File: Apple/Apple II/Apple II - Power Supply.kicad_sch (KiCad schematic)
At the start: 0 parts

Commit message: Working on Apple II - Sheet 23
My eyes said I need a break :smile:
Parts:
- added C1, C2: C_Polarized_Small, symbol Device:C_Polarized_Small
- added C23, C3, C4, C5: C_Small, symbol Device:C_Small
- added CR1: CR1_BRIDGE_RECTIFIER, symbol Apple II:CR1_BRIDGE_RECTIFIER
- added CR2, CR3: D_Filled, symbol Device:D_Filled
- added FU1: Fuse, symbol Device:Fuse
- added LF?: LINE_FILTER, symbol Apple II:LINE_FILTER
- added Q3: 2N2219, Package_TO_SOT_THT:TO-39-3, symbol Transistor_BJT:2N2219
- added R1, R2, R23, R3, R4: R_US, symbol Device:R_US
- added TR?: TR0001_TRANSFORMER, symbol Apple II:TR0001_TRANSFORMER
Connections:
- new net: C1.2, C2.2, C3.2, CR1., CR2.1 (K)
- new net: CR2.2 (A), R2.2, R3.1
- new net: C23.1, R23.1
- new net: R23.2, TR?.
- new net: Q3.1 (E), R3.2
- new net: C4.2, Q3.3 (C), TR?.
- new net: C3.1, CR3.1 (K), FU1.2, R4.2, TR?.
- new net: C23.2, CR3.2 (A), TR?.
- new net: C4.1, R4.1
- new net: C1.1, C2.1, CR1., FU1.1
- new net: C5.1, CR1., LF?.
- new net: C5.2, R2.1
- new net: LF?., R1.1
- new net: CR1., R1.2
- new net AC: LF?.
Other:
- title: (none) -> Apple II - Power Supply

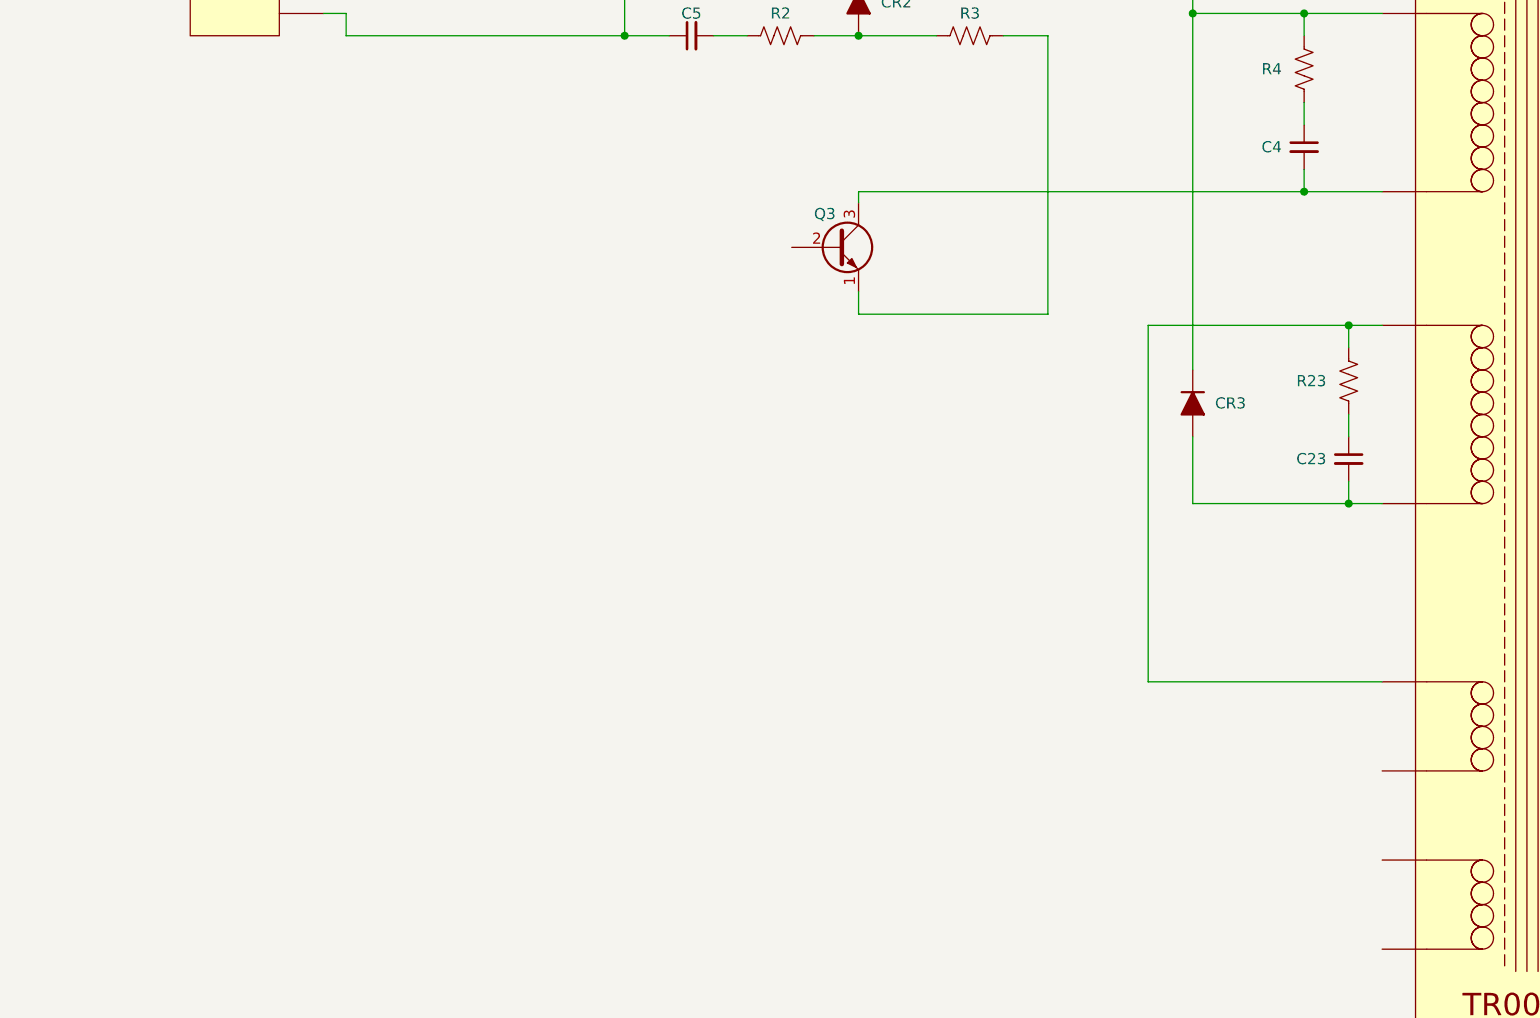
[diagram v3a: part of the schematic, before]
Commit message: Working on the Apple II Sheet 23
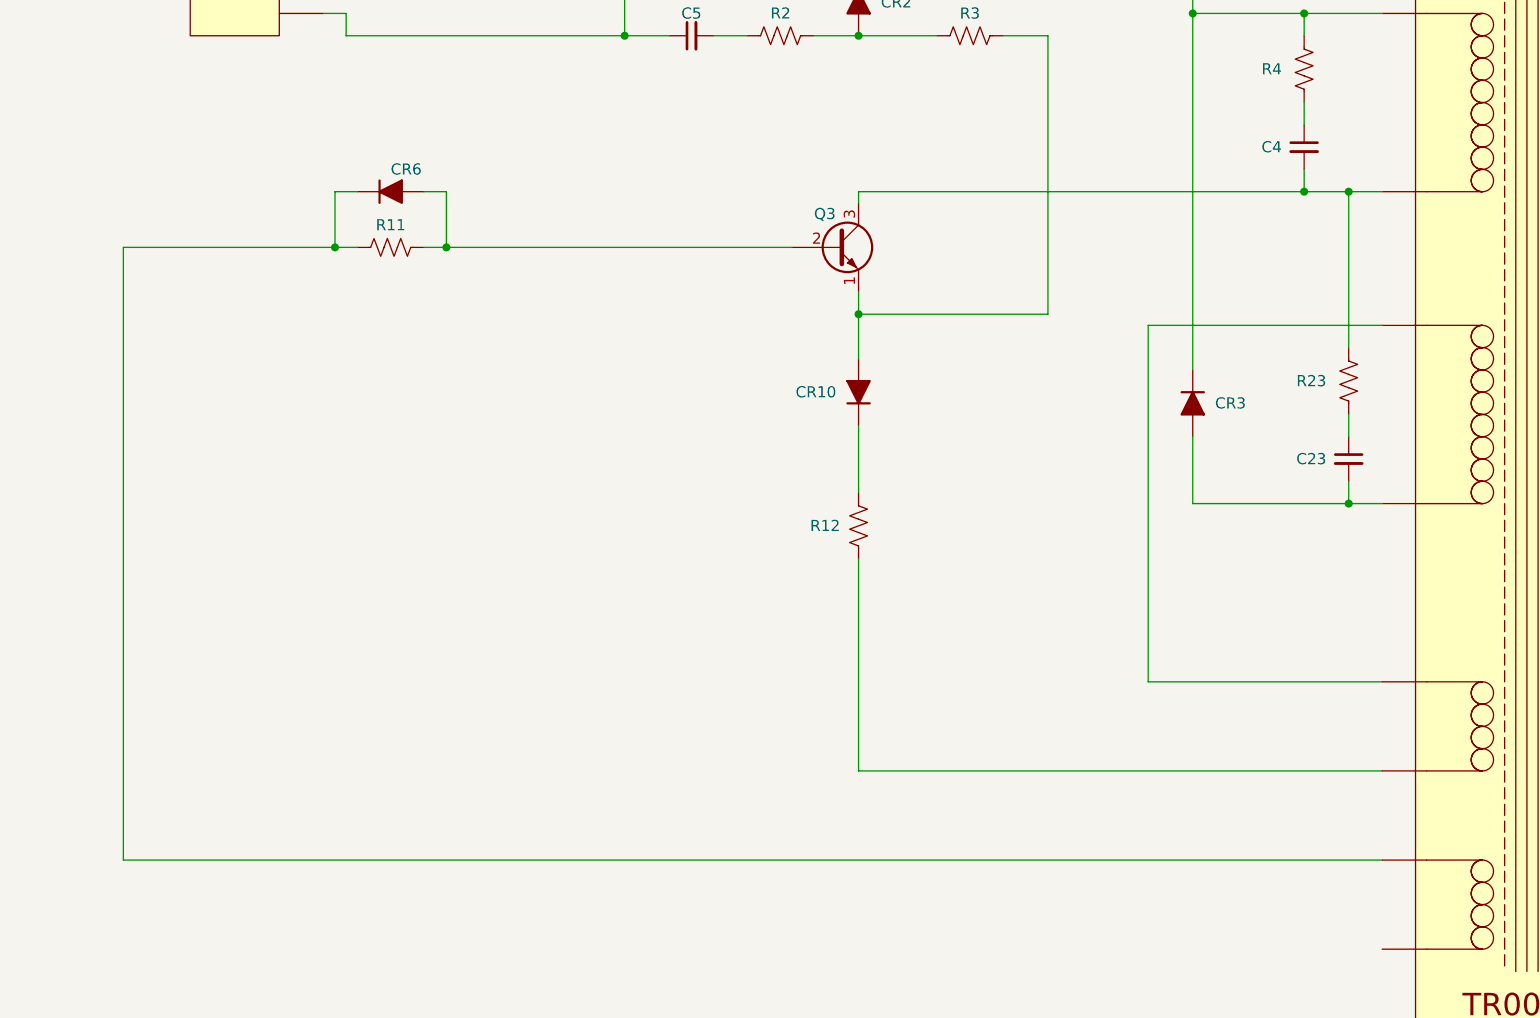
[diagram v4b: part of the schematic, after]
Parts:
- added CR10, CR6: D_Filled, symbol Device:D_Filled
- added R11, R12: R_US, symbol Device:R_US
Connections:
- net at R23.2, TR?.: now also C4.2, Q3.3 (C)
- net at Q3.1 (E), R3.2: now also CR10.2 (A)
- net at Q3.2 (B): now also CR6.2 (A), R11.2
- net at TR?.: now also CR6.1 (K), R11.1
- new net: R12.1, TR?.
- new net: CR10.1 (K), R12.2
- new net: C5.1, CR1., LF?.
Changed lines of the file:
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@@
   (junction (at 109.22 81.28) (diameter 0) (color 0 0 0 0)
   )
+  (junction (at 62.23 115.57) (diameter 0) (color 0 0 0 0)
+  )
   (junction (at 165.1 144.78) (diameter 0) (color 0 0 0 0)
   )
   (junction (at 114.3 66.04) (diameter 0) (color 0 0 0 0)
   )
+  (junction (at 109.22 123.19) (diameter 0) (color 0 0 0 0)
+  )
+  (junction (at 165.1 109.22) (diameter 0) (color 0 0 0 0)
+  )
   (junction (at 82.55 91.44) (diameter 0) (color 0 0 0 0)
   )
@@
   (junction (at 114.3 81.28) (diameter 0) (color 0 0 0 0)
   )
-  (junction (at 165.1 124.46) (diameter 0) (color 0 0 0 0)
+  (junction (at 49.53 115.57) (diameter 0) (color 0 0 0 0)
   )
   (wire (pts (xy 50.8 66.04) (xy 53.34 66.04))
@@
     (stroke (width 0) (type default) (color 0 0 0 0))
   )
+  (wire (pts (xy 52.07 115.57) (xy 49.53 115.57))
+    (stroke (width 0) (type default) (color 0 0 0 0))
+  )
   (wire (pts (xy 147.32 76.2) (xy 147.32 66.04))
     (stroke (width 0) (type default) (color 0 0 0 0))
   )
+  (wire (pts (xy 109.22 175.26) (xy 109.22 151.13))
+    (stroke (width 0) (type default) (color 0 0 0 0))
+  )
   (wire (pts (xy 50.8 68.58) (xy 48.26 68.58))
     (stroke (width 0) (type default) (color 0 0 0 0))
@@
     (stroke (width 0) (type default) (color 0 0 0 0))
   )
+  (wire (pts (xy 62.23 115.57) (xy 59.69 115.57))
+    (stroke (width 0) (type default) (color 0 0 0 0))
+  )
   (wire (pts (xy 123.19 81.28) (xy 133.35 81.28))
     (stroke (width 0) (type default) (color 0 0 0 0))
@@
     (stroke (width 0) (type default) (color 0 0 0 0))
   )
+  (wire (pts (xy 52.07 109.22) (xy 49.53 109.22))
+    (stroke (width 0) (type default) (color 0 0 0 0))
+  )
   (wire (pts (xy 125.73 91.44) (xy 130.81 91.44))
     (stroke (width 0) (type default) (color 0 0 0 0))
@@
     (stroke (width 0) (type default) (color 0 0 0 0))
   )
+  (wire (pts (xy 25.4 185.42) (xy 168.91 185.42))
+    (stroke (width 0) (type default) (color 0 0 0 0))
+  )
   (wire (pts (xy 168.91 76.2) (xy 147.32 76.2))
     (stroke (width 0) (type default) (color 0 0 0 0))
   )
+  (wire (pts (xy 59.69 109.22) (xy 62.23 109.22))
+    (stroke (width 0) (type default) (color 0 0 0 0))
+  )
   (wire (pts (xy 50.8 66.04) (xy 50.8 68.58))
     (stroke (width 0) (type default) (color 0 0 0 0))
@@
     (stroke (width 0) (type default) (color 0 0 0 0))
   )
+  (wire (pts (xy 101.6 115.57) (xy 62.23 115.57))
+    (stroke (width 0) (type default) (color 0 0 0 0))
+  )
   (wire (pts (xy 147.32 88.9) (xy 160.02 88.9))
     (stroke (width 0) (type default) (color 0 0 0 0))
@@
     (stroke (width 0) (type default) (color 0 0 0 0))
   )
+  (wire (pts (xy 168.91 175.26) (xy 109.22 175.26))
+    (stroke (width 0) (type default) (color 0 0 0 0))
+  )
   (wire (pts (xy 82.55 91.44) (xy 50.8 91.44))
     (stroke (width 0) (type default) (color 0 0 0 0))
@@
     (stroke (width 0) (type default) (color 0 0 0 0))
   )
+  (wire (pts (xy 49.53 115.57) (xy 25.4 115.57))
+    (stroke (width 0) (type default) (color 0 0 0 0))
+  )
+  (wire (pts (xy 109.22 128.27) (xy 109.22 123.19))
+    (stroke (width 0) (type default) (color 0 0 0 0))
+  )
   (wire (pts (xy 109.22 123.19) (xy 109.22 120.65))
     (stroke (width 0) (type default) (color 0 0 0 0))
   )
-  (wire (pts (xy 168.91 109.22) (xy 160.02 109.22))
+  (wire (pts (xy 168.91 109.22) (xy 165.1 109.22))
     (stroke (width 0) (type default) (color 0 0 0 0))
   )
@@
     (stroke (width 0) (type default) (color 0 0 0 0))
   )
-  (wire (pts (xy 168.91 124.46) (xy 165.1 124.46))
+  (wire (pts (xy 142.24 124.46) (xy 168.91 124.46))
     (stroke (width 0) (type default) (color 0 0 0 0))
   )
@@
     (stroke (width 0) (type default) (color 0 0 0 0))
   )
-  (wire (pts (xy 165.1 124.46) (xy 142.24 124.46))
+  (wire (pts (xy 25.4 115.57) (xy 25.4 185.42))
     (stroke (width 0) (type default) (color 0 0 0 0))
   )
@@
     (stroke (width 0) (type default) (color 0 0 0 0))
   )
+  (wire (pts (xy 49.53 109.22) (xy 49.53 115.57))
+    (stroke (width 0) (type default) (color 0 0 0 0))
+  )
   (wire (pts (xy 147.32 88.9) (xy 147.32 129.54))
     (stroke (width 0) (type default) (color 0 0 0 0))
@@
     (stroke (width 0) (type default) (color 0 0 0 0))
   )
+  (wire (pts (xy 165.1 109.22) (xy 165.1 127))
+    (stroke (width 0) (type default) (color 0 0 0 0))
+  )
+  (wire (pts (xy 165.1 109.22) (xy 160.02 109.22))
+    (stroke (width 0) (type default) (color 0 0 0 0))
+  )
   (wire (pts (xy 67.31 81.28) (xy 109.22 81.28))
     (stroke (width 0) (type default) (color 0 0 0 0))
@@
     (stroke (width 0) (type default) (color 0 0 0 0))
   )
+  (wire (pts (xy 62.23 109.22) (xy 62.23 115.57))
+    (stroke (width 0) (type default) (color 0 0 0 0))
+  )
+  (wire (pts (xy 109.22 143.51) (xy 109.22 135.89))
+    (stroke (width 0) (type default) (color 0 0 0 0))
+  )
   (wire (pts (xy 82.55 78.74) (xy 82.55 91.44))
     (stroke (width 0) (type default) (color 0 0 0 0))
   )
   (wire (pts (xy 50.8 91.44) (xy 50.8 88.9))
-    (stroke (width 0) (type default) (color 0 0 0 0))
-  )
-  (wire (pts (xy 165.1 127) (xy 165.1 124.46))
     (stroke (width 0) (type default) (color 0 0 0 0))
   )
@@
     (pin "")
   )
+  (symbol (lib_id "Device:D_Filled") (at 109.22 132.08 90) (unit 1)
+    (in_bom yes) (on_board yes)
+    (property "Reference" "CR10" (id 0) (at 106.68 132.08 90)
+      (effects (font (size 1.27 1.27)) (justify left))
+    )
+    (property "Value" "D_Filled" (id 1) (at 106.68 130.8101 90)
+      (effects (font (size 1.27 1.27)) (justify left) hide)
+    )
+    (property "Footprint" "" (id 2) (at 109.22 132.08 0)
+      (effects (font (size 1.27 1.27)) hide)
+    )
+    (property "Datasheet" "~" (id 3) (at 109.22 132.08 0)
+      (effects (font (size 1.27 1.27)) hide)
+    )
+    (pin "1")
+    (pin "2")
+  )
   (symbol (lib_id "Device:R_US") (at 160.02 95.25 180) (unit 1)
     (in_bom yes) (on_board yes)
@@
     )
     (property "Datasheet" "~" (id 3) (at 133.35 72.39 0)
+      (effects (font (size 1.27 1.27)) hide)
+    )
+    (pin "1")
+    (pin "2")
+  )
+  (symbol (lib_id "Device:R_US") (at 109.22 147.32 180) (unit 1)
+    (in_bom yes) (on_board yes)
+    (property "Reference" "R12" (id 0) (at 105.41 147.32 0))
+    (property "Value" "R_US" (id 1) (at 105.41 147.32 90)
+      (effects (font (size 1.27 1.27)) hide)
+    )
+    (property "Footprint" "" (id 2) (at 108.204 147.066 90)
+      (effects (font (size 1.27 1.27)) hide)
+    )
+    (property "Datasheet" "~" (id 3) (at 109.22 147.32 0)
       (effects (font (size 1.27 1.27)) hide)
     )
@@
     (pin "1")
   )
+  (symbol (lib_id "Device:R_US") (at 55.88 115.57 90) (unit 1)
+    (in_bom yes) (on_board yes)
+    (property "Reference" "R11" (id 0) (at 55.88 113.03 90))
+    (property "Value" "R_US" (id 1) (at 55.88 111.76 90)
+      (effects (font (size 1.27 1.27)) hide)
+    )
+    (property "Footprint" "" (id 2) (at 56.134 114.554 90)
+      (effects (font (size 1.27 1.27)) hide)
+    )
+    (property "Datasheet" "~" (id 3) (at 55.88 115.57 0)
+      (effects (font (size 1.27 1.27)) hide)
+    )
+    (pin "1")
+    (pin "2")
+  )
   (symbol (lib_id "Device:D_Filled") (at 147.32 133.35 270) (unit 1)
     (in_bom yes) (on_board yes)
@@
     (pin "")
   )
+  (symbol (lib_id "Device:D_Filled") (at 55.88 109.22 0) (unit 1)
+    (in_bom yes) (on_board yes)
+    (property "Reference" "CR6" (id 0) (at 55.88 106.68 0)
+      (effects (font (size 1.27 1.27)) (justify left))
+    )
+    (property "Value" "D_Filled" (id 1) (at 57.1499 106.68 90)
+      (effects (font (size 1.27 1.27)) (justify left) hide)
+    )
+    (property "Footprint" "" (id 2) (at 55.88 109.22 0)
+      (effects (font (size 1.27 1.27)) hide)
+    )
+    (property "Datasheet" "~" (id 3) (at 55.88 109.22 0)
+      (effects (font (size 1.27 1.27)) hide)
+    )
+    (pin "1")
+    (pin "2")
+  )
   (symbol (lib_id "Apple II:CR1_BRIDGE_RECTIFIER") (at 74.93 72.39 0) (unit 1)

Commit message: More Apple II Power Supply work
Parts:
- added *AR1: AR1_Amplifier, symbol Apple II:AR1_Amplifier
- added C10, C11, C22, C6, C7: C_Polarized_Small, symbol Device:C_Polarized_Small
- added C8, C9: C_Small, symbol Device:C_Small
- added CR11, CR12, CR13, CR14, CR15, CR16, CR7, CR9: D_Filled, symbol Device:D_Filled
- added CR5: D_Schottky, symbol Device:D_Schottky_Filled
- added L1, L2, L3, L4: L_Iron, symbol Device:L_Iron
- added Q1: 2N2219, Package_TO_SOT_THT:TO-39-3, symbol Transistor_BJT:2N2219
- added Q2: 2N3906, Package_TO_SOT_THT:TO-92_Inline, symbol Transistor_BJT:2N3906
- added R10, R13, R14, R22, R5, R6, R8, R9: R_US, symbol Device:R_US
- added U? (x2): Wierd_Transformer_Connection, symbol Apple II:Wierd_Transformer_Connection
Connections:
- net at C1.2, C2.2, C3.2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: now also TR?., C22.2, C6.1, C7.2, C9.2, Q1.1 (E), Q2.3 (C), R13.1, R6.2, U?., U?.
- net at CR10.2 (A), Q3.1 (E), R3.2: now also C9.1, R22.1
- net at CR6.2 (A), Q3.2 (B), R11.2: now also CR7.2 (A)
- net BLK (GND): now reaches TR?.
- net at R12.1, TR?.: now also R13.2, R9.2
- new net: C10.2, C11.1, CR13.1 (K), TR?.
- new net: C11.2, TR?.
- new net: CR16.1 (K), TR?.
- new net: CR16.2 (A), L4.1
- new net: CR7.1 (K), Q2.1 (E), R10.2
- new net: Q1.3 (C), Q2.2 (B), R10.1
- new net: CR15.2 (A), L3.1
- new net: CR14.2 (A), TR?.
- new net: R5.1, TR?.
- new net: CR15.1 (K), TR?.
- new net: CR12.2 (A), TR?.
- new net: CR13.2 (A), TR?.
- new net: CR14.1 (K), L2.1
- new net: *AR1.1, C6.2, C8.2, CR9.2 (A)
- new net: *AR1.2, C8.1
- new net: *AR1.3, R14.1
- new net: C7.1, CR11.1 (K), CR5.1 (K)
- new net: CR11.2 (A), CR9.1 (K), R5.2
- new net: CR5.2 (A), R6.1, R8.1
- new net: Q1.2 (B), R14.2, R8.2, R9.1
- new net: C5.1, CR1., LF?.
- new net: C10.1, CR12.1 (K), L1.1
- new net: C22.1, R22.2
- new net BLU (-5V): L3.2
- new net BLU/WHT (-12V): L4.2
- new net ORG (+5V): L2.2
- new net ORG/WHT (+12V): L1.2
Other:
- moved on the sheet: C3, CR10, CR3

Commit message: Apple II Complete!
All done!  Release to follow!
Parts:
- added AR1: AR1_Amplifier, symbol Apple II:AR1_Amplifier
- added C12, C13, C14, C16, C17, C18, C19, C20: C_Polarized_Small, symbol Device:C_Polarized_Small
- added C21: C_Small, symbol Device:C_Small
- added C?: CONN_PSU, symbol Apple II:CONN_PSU
- added CR17, CR18: D_Filled, symbol Device:D_Filled
- added CR19, CR20: D_Schottky, symbol Device:D_Schottky_Filled
- added Q4: 2N2219, Package_TO_SOT_THT:TO-39-3, symbol Transistor_BJT:2N2219
- added Q5: Q5, symbol Apple II:Q5
- added R15, R17, R18, R19, R20, R21, R24, R25, R26, R27: R_US, symbol Device:R_US
- added R16: R_Potentiometer_US, symbol Device:R_Potentiometer_US
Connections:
- net BLK (GND) is gone; now on an unnamed net: TR?.
- net at C1.2, C2.2, C22.2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: now also CR6.1 (K), R11.1, R12.1, R13.2, R5.1, R9.2
- net at C10.2, C11.1, CR13.1 (K)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: now also CR14.1 (K), L2.1, C12.1, R17.1
- net at C11.2, TR?.: now also C12.2, C13.1, C16.2, C17.2, C18.2, C19.1, C20.1, C21.2, C?.3 (BLK), C?.4 (BLK), CR19.2 (A), Q5.3, R21.1, R24.1, R26.1
- net at CR16.2 (A), L4.1: now also C14.2
- net at CR15.2 (A), L3.1: now also TR?., C13.2, C14.1
- net at TR?.: now also CR13.2 (A)
- net BLU (-5V): no longer names the net of L3.2
- net BLU (-5V): now also C19.2, C?.5 (BLU), R26.2
- net BLU/WHT (-12V): no longer names the net of L4.2
- net BLU/WHT (-12V): now also C20.2, C?.6 (BLU/WHT), R25.2
- net ORG (+5V): no longer names the net of L2.2
- net ORG (+5V): now also C18.1, C?.2 (ORG), R20.2
- net ORG/WHT (+12V): no longer names the net of L1.2
- net ORG/WHT (+12V): now also AR1.2, C17.1, C?.1 (ORG/WHT), CR20.1 (K), R15.1, R16.1, R18.1
- new net: Q5.2, R21.2
- new net: R24.2, R25.1
- new net: Q4.3 (C), R18.2, R19.2
- new net: CR18.1 (K), CR19.1 (K), R16.3
- new net: CR17.1 (K), CR18.2 (A)
- new net: Q4.1 (E), R17.2, R20.1
- new net: C16.1, Q4.2 (B), R16.2
- new net: CR20.2 (A), R27.1
- new net: AR1.1, R19.1
- new net: C5.1, CR1., LF?.
- new net: CR17.2 (A), R15.2
- new net: Q5.1, R27.2
- new net Earth: C21.1
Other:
- moved on the sheet: *AR1A, C1, C10, C11, C2, C22, C23, C3, C4, C5, C6, C7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
